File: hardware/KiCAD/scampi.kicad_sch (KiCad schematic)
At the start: 57 parts, among them IC1 LSF0204GU12X, J2 PJ-320D, U1 MIC5365-1.8YC5-TR, U2 TLV320AIC3100, U3 ATTINY1616-MNR

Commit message: layout changes, ADC test fw
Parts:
- removed J2: PJ-320D, SamacSys_Parts:Jack_3.5mm_PJ320D_Horizontal, symbol Connector_Audio:AudioJack4
- removed R2: 100k, Resistor_SMD:R_0402_1005Metric, symbol Device:R_Small
- added DET1, HPL1, HPR1: ~, SamacSys_Parts:pth_pad, symbol Connector:TestPoint
- added J1: AudioJack3_SwitchT, Connector_Audio:Jack_3.5mm_CUI_SJ-3524-SMT_Horizontal, symbol Connector_Audio:AudioJack3_SwitchT
- renumbered C16 to C13, C17 to C14, C18 to C15, C13 to C16, C14 to C17, C15 to C18, R3 to R2, R4 to R3, R1 to R4, TP5 to TP1, TP14 to TP10, TP15 to TP11, TP16 to TP12, TP17 to TP13, TP18 to TP14, TP1 to TP15, TP2 to TP16, TP3 to TP17, TP4 to TP18, TP6 to TP2, TP7 to TP3, TP8 to TP4, TP9 to TP5, TP10 to TP6, TP11 to TP7, TP12 to TP8, TP13 to TP9
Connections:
- net GND: now also J1.S; no longer U3.11 (PB3)
- net HPL: now also HPL1.1, J1.T
- net HPR: now also HPR1.1, J1.R
- net HPS: now also U3.11 (PB3), DET1.1, J1.TN; no longer U2.11 (VOL/MICDET)
- no-connect marks 5 -> 7

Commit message: finalize layout, add gerbers and step file
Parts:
- removed DET1: ~, SamacSys_Parts:pth_pad, symbol Connector:TestPoint
- removed J1: AudioJack3_SwitchT, Connector_Audio:Jack_3.5mm_CUI_SJ-3524-SMT_Horizontal, symbol Connector_Audio:AudioJack3_SwitchT
- added J1: PJ320D Pink, SamacSys_Parts:Jack_3.5mm_PJ320D_Horizontal, symbol Connector_Audio:AudioJack4
- added R2: 4.7k, Resistor_SMD:R_0402_1005Metric, symbol Device:R_Small
- added SENSE1: ~, SamacSys_Parts:pth_pad, symbol Connector:TestPoint
- added TP11: GND, SamacSys_Parts:TestPoint_Pad_D0.75, symbol Connector:TestPoint
- R1: renamed from R4; value 100k -> 4.7k
- UPDI1: value UPDI -> (none)
- renumbered C16 to C13, C17 to C14, C18 to C15, C13 to C16, C14 to C17, C15 to C18, R2 to R3, R3 to R4, TP15 to TP1, TP6 to TP10, TP7 to TP12, TP8 to TP13, TP9 to TP14, TP10 to TP15, TP11 to TP16, TP12 to TP17, TP13 to TP18, TP14 to TP19, TP16 to TP2, TP17 to TP3, TP18 to TP4, TP1 to TP5, TP2 to TP6, TP3 to TP7, TP4 to TP8, TP5 to TP9, IC1 to U1, U1 to U2, U2 to U3, U3 to U4
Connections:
- net +1V8: now also TP11.1
- net GND: now also U4.11 (PB3), J1.S
- net HPL: now also J1.T
- net HPR: now also J1.R1
- net HPS: now also U3.11 (VOL/MICDET), J1.R2, R2.1, SENSE1.1; no longer U4.11 (PB3)
- net at U3.12 (MICBIAS): now also R2.2
- no-connect marks 7 -> 5

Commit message: finalize layout!
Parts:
- added JP5: SolderJumper_2_Open, SamacSys_Parts:small_solder_jumper, symbol Jumper:SolderJumper_2_Open
- UPDI1: value (none) -> ~
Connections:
- net GND: now also JP5.2 (B); no longer U4.17 (PC2)
- new net: JP5.1 (A), U4.17 (PC2)
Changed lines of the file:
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@@
 	)
 	(junction
-		(at 208.28 83.82)
-		(diameter 0)
-		(color 0 0 0 0)
-	)
-	(junction
 		(at 208.28 71.12)
 		(diameter 0)
@@
 	(wire
 		(pts
+			(xy 196.85 83.82) (xy 198.12 83.82)
+		)
+		(stroke
+			(width 0)
+			(type default)
+		)
+	)
+	(wire
+		(pts
 			(xy 257.81 74.93) (xy 257.81 77.47)
 		)
@@
 	(wire
 		(pts
-			(xy 208.28 83.82) (xy 210.82 83.82)
-		)
-		(stroke
-			(width 0)
-			(type default)
-		)
-	)
-	(wire
-		(pts
 			(xy 80.01 99.06) (xy 105.41 99.06)
 		)
@@
 	(wire
 		(pts
-			(xy 208.28 83.82) (xy 208.28 86.36)
+			(xy 208.28 73.66) (xy 208.28 86.36)
 		)
 		(stroke
@@
 	(wire
 		(pts
+			(xy 205.74 83.82) (xy 210.82 83.82)
+		)
+		(stroke
+			(width 0)
+			(type default)
+		)
+	)
+	(wire
+		(pts
 			(xy 256.54 72.39) (xy 267.97 72.39)
 		)
@@
 	(wire
 		(pts
+			(xy 196.85 90.17) (xy 196.85 83.82)
+		)
+		(stroke
+			(width 0)
+			(type default)
+		)
+	)
+	(wire
+		(pts
 			(xy 210.82 68.58) (xy 208.28 68.58)
 		)
@@
 	(wire
 		(pts
-			(xy 208.28 73.66) (xy 208.28 83.82)
-		)
-		(stroke
-			(width 0)
-			(type default)
-		)
-	)
-	(wire
-		(pts
 			(xy 101.6 86.36) (xy 105.41 86.36)
 		)
@@
 	)
 	(symbol
+		(lib_id "power:GND")
+		(at 196.85 90.17 0)
+		(unit 1)
+		(exclude_from_sim no)
+		(in_bom yes)
+		(on_board yes)
+		(dnp no)
+		(fields_autoplaced yes)
+		(property "Reference" "#PWR041"
+			(at 196.85 96.52 0)
+			(effects
+				(font
+					(size 1.27 1.27)
+				)
+				(hide yes)
+			)
+		)
+		(property "Value" "GND"
+			(at 196.85 95.25 0)
+			(effects
+				(font
+					(size 1.27 1.27)
+				)
+				(hide yes)
+			)
+		)
+		(property "Footprint" ""
+			(at 196.85 90.17 0)
+			(effects
+				(font
+					(size 1.27 1.27)
+				)
+				(hide yes)
+			)
+		)
+		(property "Datasheet" ""
+			(at 196.85 90.17 0)
+			(effects
+				(font
+					(size 1.27 1.27)
+				)
+				(hide yes)
+			)
+		)
+		(property "Description" ""
+			(at 196.85 90.17 0)
+			(effects
+				(font
+					(size 1.27 1.27)
+				)
+				(hide yes)
+			)
+		)
+		(property "MPN" ""
+			(at 196.85 90.17 0)
+			(effects
+				(font
+					(size 1.27 1.27)
+				)
+				(hide yes)
+			)
+		)
+		(property "Digi-Key Part #" ""
+			(at 196.85 90.17 0)
+			(effects
+				(font
+					(size 1.27 1.27)
+				)
+				(hide yes)
+			)
+		)
+		(pin "1"
+		)
+		(instances
+			(project "scampi"
+				(path "/cabc36b8-f44e-4129-b157-2e140b6b20b4"
+					(reference "#PWR041")
+					(unit 1)
+				)
+			)
+		)
+	)
+	(symbol
 		(lib_id "Connector:TestPoint")
 		(at 148.59 73.66 270)
@@
 			)
 		)
-		(property "Value" ""
+		(property "Value" "~"
 			(at 264.922 64.77 0)
 			(effects
@@
 					(unit 1)
 				)
+			)
+		)
+	)
+	(symbol
+		(lib_id "Jumper:SolderJumper_2_Open")
+		(at 201.93 83.82 0)
+		(mirror y)
+		(unit 1)
+		(exclude_from_sim no)
+		(in_bom yes)
+		(on_board yes)
+		(dnp no)
+		(property "Reference" "JP5"
+			(at 202.184 81.28 0)
+			(effects
+				(font
+					(size 1.27 1.27)
+				)
+				(hide yes)
+			)
+		)
+		(property "Value" "SolderJumper_2_Open"
+			(at 201.93 80.01 0)
+			(effects
+				(font
+					(size 1.27 1.27)
+				)
+				(hide yes)
+			)
+		)
+		(property "Footprint" "SamacSys_Parts:small_solder_jumper"
+			(at 201.93 83.82 0)
+			(effects
+				(font
+					(size 1.27 1.27)
+				)
+				(hide yes)
+			)
+		)
+		(property "Datasheet" "~"
+			(at 201.93 83.82 0)
+			(effects
+				(font
+					(size 1.27 1.27)
+				)
+				(hide yes)
+			)
+		)
+		(property "Description" "Solder Jumper, 2-pole, open"
+			(at 201.93 83.82 0)
+			(effects
+				(font
+					(size 1.27 1.27)
+				)
+				(hide yes)
+			)
+		)
+		(pin "1"
+		)
+		(pin "2"
+		)
+		(instances
+			(project "scampi"
+				(path "/cabc36b8-f44e-4129-b157-2e140b6b20b4"
+					(reference "JP5")
+					(unit 1)
+				)

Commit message: add bom, embed fonts + 3d
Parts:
- TP13: renamed from SPKL+1; value ~ -> SPKL+
- TP14: renamed from SPKL-1; value ~ -> SPKL-
- TP15: renamed from SPKR-1; value ~ -> SPKR-
- TP16: renamed from SPKR+1; value ~ -> SPKR+
- TP17: renamed from SPVDD1; value ~ -> SPVDD
- TP18: renamed from HPL1; value ~ -> HPL
- TP19: renamed from HPR1; value ~ -> HPR
- TP20: renamed from SENSE1; value ~ -> HPS
- TP25: renamed from VOL+1; value ~ -> VOL+
- TP26: renamed from VOL-1; value ~ -> VOL-
- TP27: renamed from TP17; value V+ -> 3.3V
- TP28: renamed from UPDI1; value ~ -> UPDI
- U1: value LSF0204GU12X -> TXU0104RUTR; footprint SamacSys_Parts:LSF0204GU12X -> SamacSys:UQFN-12; Manufacturer_Name Nexperia -> TI; Manufacturer_Part_Number LSF0204GU12X -> TXU0104RUTR; Mouser Part Number 771-LSF0204GU12X -> TXU0104RUTR; Mouser Price/Stock https://www.mouser.co.uk/ProductDetail/Nexperia/LSF0204GU12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 -> (none)
- renumbered JP5 to JP1, JP1 to JP2, JP2 to JP3, JP3 to JP4, JP4 to JP5, TP13 to TP21, TP14 to TP22, TP15 to TP23, TP16 to TP24, TP18 to TP29, TP19 to TP30
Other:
- moved on the sheet: J1, TP4

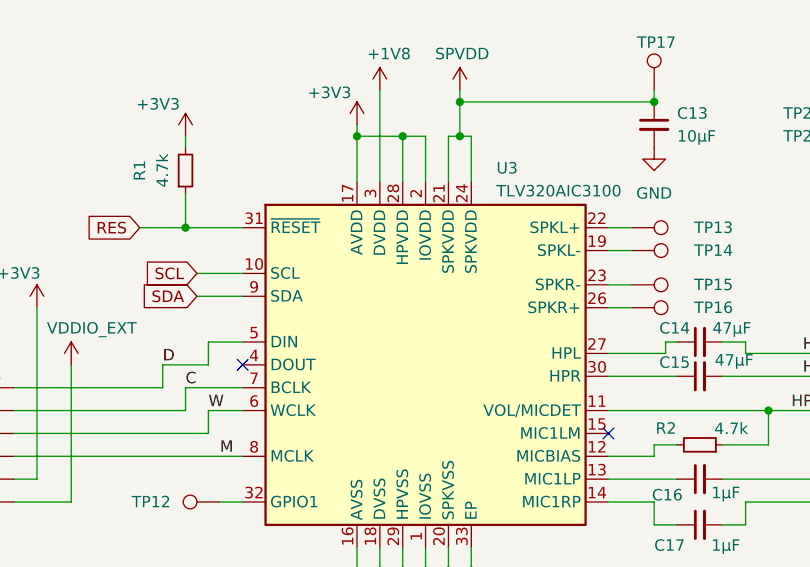
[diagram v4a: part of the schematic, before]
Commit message: Add schematic pdf
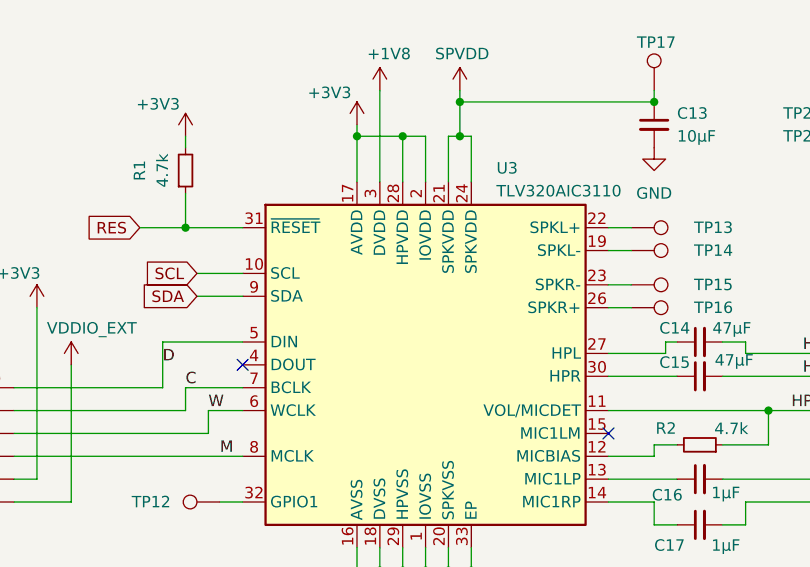
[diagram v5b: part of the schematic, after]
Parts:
- TP1, TP10, TP12, TP2, TP21, TP22, TP3, TP4, TP5, TP6, TP7, TP8, TP9: value ~ -> (none)
- U3: value TLV320AIC3100 -> TLV320AIC3110

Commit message: Update schematic
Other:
- note added: "Scampi"
- note added: "truly universal shrimp-themed digital audio amp for portablizers"
- moved on the sheet: C10, C11, C12, C13, C14, C15, C16, C17, C18, C2, C3, C5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
